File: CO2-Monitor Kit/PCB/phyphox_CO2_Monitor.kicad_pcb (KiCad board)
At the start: 2 copper layers, 73 x 42 mm, 15 parts, among them J1 Conn_01x19_Female, J2 Conn_01x19_Female, J3 Conn_01x05_Female, U1 ESP32-DEVKITC-32D, U2 SCD30

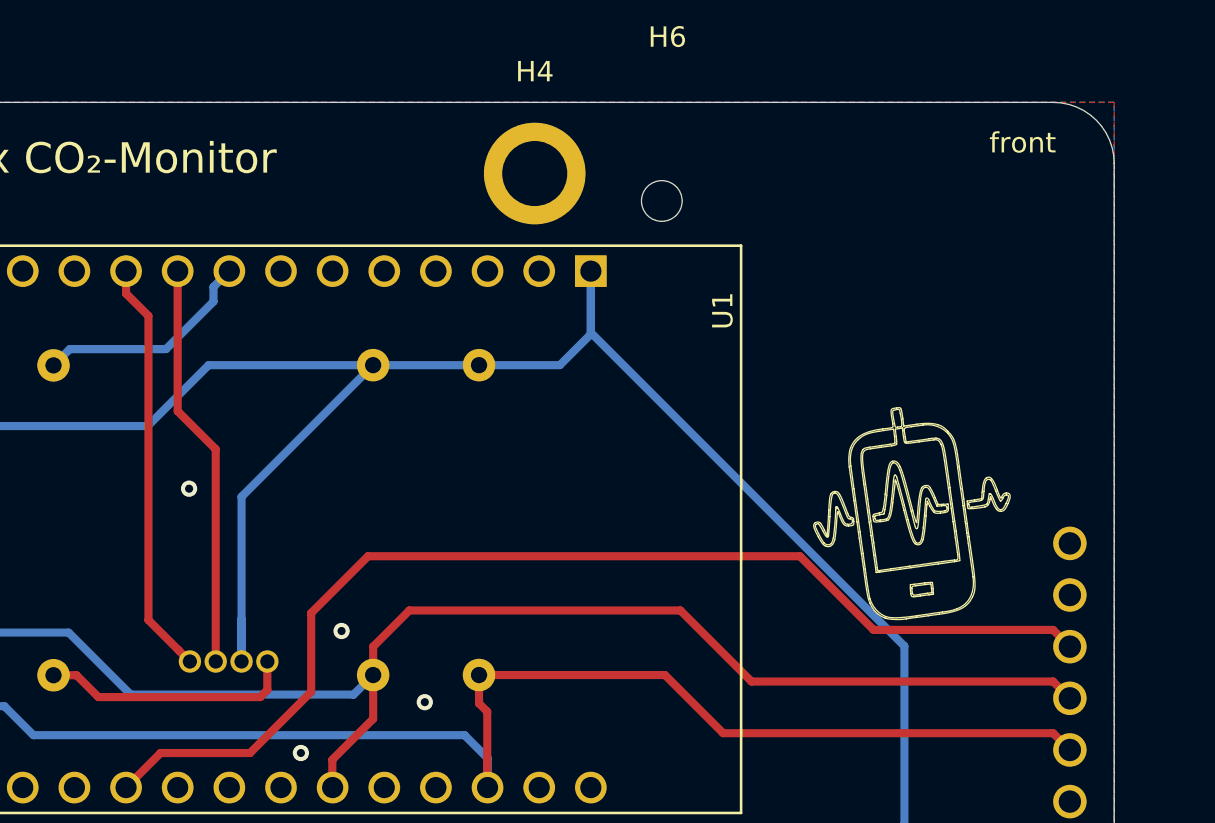
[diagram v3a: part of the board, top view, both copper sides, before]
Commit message: [CO2-Kit] Update PCB to Rev 1.1
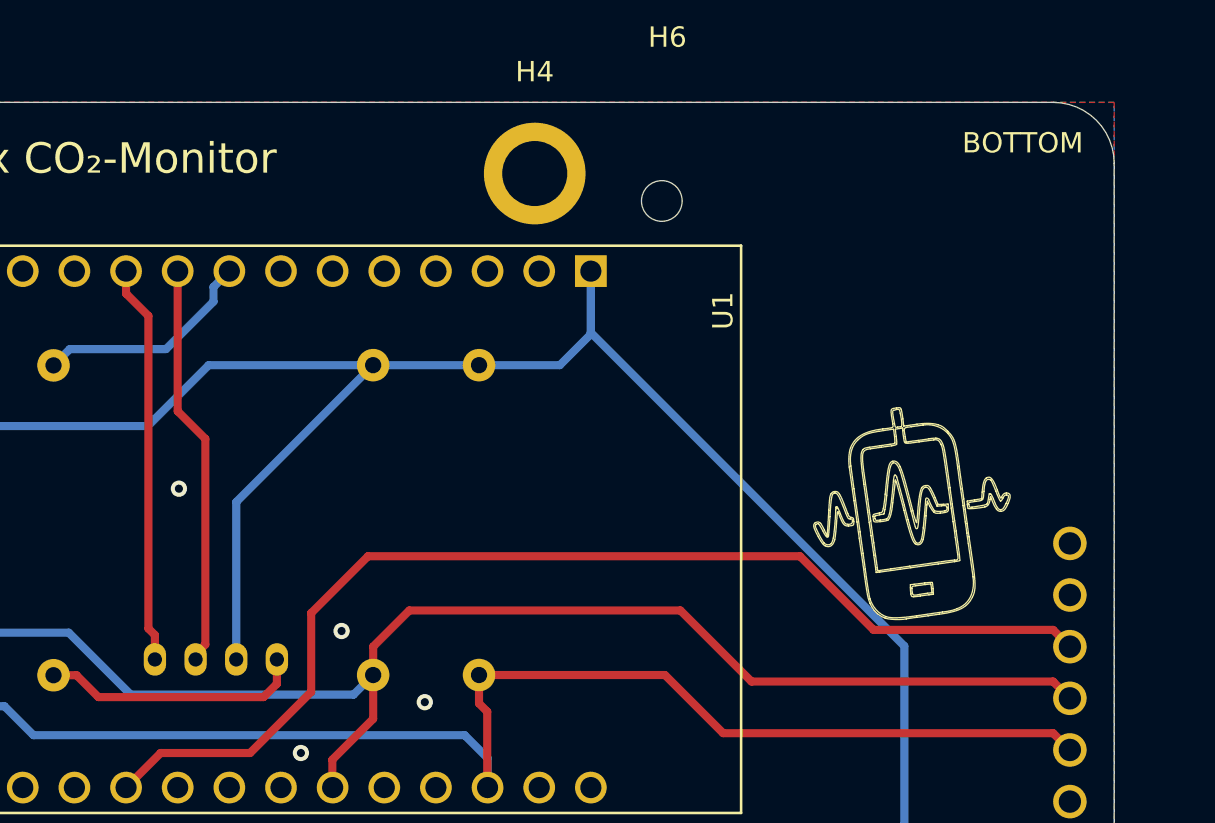
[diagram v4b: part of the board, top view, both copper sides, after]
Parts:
- D1: footprint phyphox_CO2_Monitor:WP154A4SEJ3VBDZGWCA -> phyphox_CO2_Monitor:WP154A4SEJ3VBDZGWCA_largerDistance
- moved D1 0.44 mm to (138.3, 85.1)
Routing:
- net VDD: track 109.2 -> 107.1 mm
- net GREEN: track 20.5 -> 19.7 mm
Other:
- board text added: "BOTTOM"
- board text added: "Rev 1.1"
- board text added: "TOP"
- board text removed: "Rev 1.0"
- board text removed: "back"
- board text removed: "front"
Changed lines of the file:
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@@
     (thickness 1.6)
     (drawings 608)
-    (tracks 88)
+    (tracks 90)
     (zones 0)
     (modules 15)
@@
     (add_net SDA)
     (add_net VDD)
+  )
+  (module phyphox_CO2_Monitor:WP154A4SEJ3VBDZGWCA_largerDistance (layer B.Cu)
+    (at 138.33364 85.09746 90)
+    (fp_text reference D1 (at 0 -0.5 90) (layer B.SilkS)
+      (effects (font (size 1 1) (thickness 0.15)) (justify mirror))
+    )
+    (fp_text value LED_BARG (at 0 0.5 90) (layer B.Fab)
+      (effects (font (size 1 1) (thickness 0.15)) (justify mirror))
+    )
+    (fp_line (start 2 7.999999) (end -1.999999 7.999999) (layer B.SilkS) (width 0.15))
+    (fp_arc (start 0 4.445) (end -1.999999 7.999999) (angle 301.2768412) (layer B.SilkS) (width 0.15))
+    (pad 4 thru_hole oval (at 0 1.25 90) (size 1.6 1.1) (drill 0.7) (layers *.Cu *.Mask)
+      (net 7 GREEN))
+    (pad 3 thru_hole oval (at 0 3.25 90) (size 1.6 1.1) (drill 0.7) (layers *.Cu *.Mask)
+      (net 8 BLUE))
+    (pad 2 thru_hole oval (at 0 5.25 90) (size 1.6 1.1) (drill 0.7) (layers *.Cu *.Mask)
+      (net 2 VDD))
+    (pad 1 thru_hole oval (at 0 7.25 90) (size 1.6 1.1) (drill 0.7) (layers *.Cu *.Mask)
+      (net 1 "Net-(D1-Pad1)"))
   )
   (module MountingHole:MountingHole_2mm (layer F.Cu)
@@
       (net 6 GND))
   )
-  (module phyphox_CO2_Monitor:WP154A4SEJ3VBDZGWCA (layer B.Cu)
-    (at 138.7648 85.1992 90)
-    (fp_text reference D1 (at -3.842 4.628 -90) (layer B.SilkS)
-      (effects (font (size 1 1) (thickness 0.15)) (justify mirror))
-    )
-    (fp_text value LED_BARG (at 0.36 7.65 -90) (layer B.Fab)
-      (effects (font (size 1 1) (thickness 0.15)) (justify mirror))
-    )
-    (fp_line (start 1.27 6.984999) (end -1.269999 6.984999) (layer B.SilkS) (width 0.15))
-    (fp_arc (start 0 4.445) (end -1.269999 6.984999) (angle 306.8698976) (layer B.SilkS) (width 0.15))
-    (pad 4 thru_hole circle (at 0 2.54 90) (size 1.1 1.1) (drill 0.7) (layers *.Cu *.Mask)
-      (net 7 GREEN))
-    (pad 3 thru_hole circle (at 0 3.81 90) (size 1.1 1.1) (drill 0.7) (layers *.Cu *.Mask)
-      (net 8 BLUE))
-    (pad 2 thru_hole circle (at 0 5.08 90) (size 1.1 1.1) (drill 0.7) (layers *.Cu *.Mask)
-      (net 2 VDD))
-    (pad 1 thru_hole circle (at 0 6.35 90) (size 1.1 1.1) (drill 0.7) (layers *.Cu *.Mask)
-      (net 1 "Net-(D1-Pad1)"))
-  )
   (module Connector_PinSocket_2.54mm:PinSocket_1x19_P2.54mm_Vertical (layer F.Cu)
     (at 161.2648 114.6992 270)
@@
     )
   )
-  (gr_text back (at 182.2648 59.6992) (layer B.SilkS)
+  (gr_text TOP (at 182.2648 59.6992) (layer B.SilkS)
     (effects (font (size 1 1) (thickness 0.15)) (justify mirror))
   )
-  (gr_text front (at 182.2648 59.6992) (layer F.SilkS)
+  (gr_text BOTTOM (at 182.2648 59.6992) (layer F.SilkS)
     (effects (font (size 1 1) (thickness 0.15)))
   )
@@
   (gr_curve (pts (xy 147.544591 72.77071) (xy 147.759932 72.77071) (xy 147.787269 72.922918) (xy 147.634671 73.272271)) (layer B.SilkS) (width 0.01))
   (gr_curve (pts (xy 147.634671 73.272271) (xy 147.501108 73.578043) (xy 147.414536 73.67071) (xy 147.262435 73.67071)) (layer B.SilkS) (width 0.01))
-  (gr_text "Rev 1.0" (at 150.4448 96.6592) (layer B.SilkS)
+  (gr_text "Rev 1.1" (at 150.4448 96.6592) (layer B.SilkS)
     (effects (font (size 1.5 1.5) (thickness 0.3)) (justify mirror))
   )
@@
   (segment (start 134.5973 85.8747) (end 135.72867 85.8747) (width 0.4) (layer F.Cu) (net 1))
   (segment (start 136.80317 86.9492) (end 144.7648 86.9492) (width 0.4) (layer F.Cu) (net 1))
-  (segment (start 145.1148 86.5992) (end 145.1148 85.1992) (width 0.4) (layer F.Cu) (net 1))
-  (segment (start 144.7648 86.9492) (end 145.1148 86.5992) (width 0.4) (layer F.Cu) (net 1))
+  (segment (start 144.9319 86.9492) (end 144.7648 86.9492) (width 0.4) (layer F.Cu) (net 1))
+  (segment (start 145.58364 86.29746) (end 144.9319 86.9492) (width 0.4) (layer F.Cu) (net 1))
+  (segment (start 145.58364 85.09746) (end 145.58364 86.29746) (width 0.4) (layer F.Cu) (net 1))
   (segment (start 150.3178 70.6242) (end 155.5248 70.6242) (width 0.4) (layer B.Cu) (net 2))
   (segment (start 155.5248 70.6242) (end 159.4998 70.6242) (width 0.4) (layer B.Cu) (net 2))
   (segment (start 161.0248 69.0992) (end 161.0248 65.9992) (width 0.4) (layer B.Cu) (net 2))
   (segment (start 159.4998 70.6242) (end 161.0248 69.0992) (width 0.4) (layer B.Cu) (net 2))
-  (segment (start 143.8448 83.1042) (end 143.8448 85.1992) (width 0.4) (layer B.Cu) (net 2))
-  (segment (start 143.8448 77.0972) (end 150.3178 70.6242) (width 0.4) (layer B.Cu) (net 2))
-  (segment (start 143.8448 85.1992) (end 143.8448 77.0972) (width 0.4) (layer B.Cu) (net 2))
   (segment (start 161.0248 69.0232) (end 161.0248 65.9992) (width 0.4) (layer B.Cu) (net 2))
   (segment (start 176.4448 84.4432) (end 161.0248 69.0232) (width 0.4) (layer B.Cu) (net 2))
@@
   (segment (start 142.2278 70.6242) (end 150.3178 70.6242) (width 0.4) (layer B.Cu) (net 2))
   (segment (start 139.2328 73.6192) (end 142.2278 70.6242) (width 0.4) (layer B.Cu) (net 2))
+  (segment (start 143.58364 77.35836) (end 143.58364 85.09746) (width 0.4) (layer B.Cu) (net 2))
+  (segment (start 150.3178 70.6242) (end 143.58364 77.35836) (width 0.4) (layer B.Cu) (net 2))
   (segment (start 150.3178 88.0232) (end 150.3178 85.8642) (width 0.4) (layer F.Cu) (net 3))
   (segment (start 148.31 91.376) (end 148.31 90.031) (width 0.4) (layer F.Cu) (net 3))
@@
   (via (at 152.8578 87.1992) (size 0.8) (drill 0.4) (layers F.Cu B.Cu) (net 6))
   (via (at 148.7648 83.6992) (size 0.8) (drill 0.4) (layers F.Cu B.Cu) (net 6))
-  (via (at 141.2648 76.6992) (size 0.8) (drill 0.4) (layers F.Cu B.Cu) (net 6))
+  (via (at 140.7648 76.6992) (size 0.8) (drill 0.4) (layers F.Cu B.Cu) (net 6))
   (via (at 117.2648 71.1992) (size 0.8) (drill 0.4) (layers F.Cu B.Cu) (net 6))
-  (segment (start 140.754801 84.649201) (end 141.3048 85.1992) (width 0.4) (layer F.Cu) (net 7))
-  (segment (start 139.2648 83.1592) (end 140.754801 84.649201) (width 0.4) (layer F.Cu) (net 7))
-  (segment (start 139.2648 68.202286) (end 139.2648 83.1592) (width 0.4) (layer F.Cu) (net 7))
-  (segment (start 138.1648 65.9992) (end 138.1648 67.102286) (width 0.4) (layer F.Cu) (net 7))
-  (segment (start 138.1648 67.102286) (end 139.2648 68.202286) (width 0.4) (layer F.Cu) (net 7))
-  (segment (start 142.5748 85.1992) (end 142.5748 74.7592) (width 0.4) (layer F.Cu) (net 8))
+  (segment (start 138.1648 67.102286) (end 138.1648 65.9992) (width 0.4) (layer F.Cu) (net 7))
+  (segment (start 139.2648 68.202286) (end 138.1648 67.102286) (width 0.4) (layer F.Cu) (net 7))
+  (segment (start 139.2648 83.57862) (end 139.2648 68.202286) (width 0.4) (layer F.Cu) (net 7))
+  (segment (start 139.58364 83.89746) (end 139.2648 83.57862) (width 0.4) (layer F.Cu) (net 7))
+  (segment (start 139.58364 85.09746) (end 139.58364 83.89746) (width 0.4) (layer F.Cu) (net 7))
   (segment (start 140.7048 72.8892) (end 140.7048 65.9992) (width 0.4) (layer F.Cu) (net 8))
-  (segment (start 142.5748 74.7592) (end 140.7048 72.8892) (width 0.4) (layer F.Cu) (net 8))
+  (segment (start 142.064801 74.249201) (end 140.7048 72.8892) (width 0.4) (layer F.Cu) (net 8))
+  (segment (start 142.064801 84.366299) (end 142.064801 74.249201) (width 0.4) (layer F.Cu) (net 8))
+  (segment (start 141.58364 84.84746) (end 142.064801 84.366299) (width 0.4) (layer F.Cu) (net 8))
+  (segment (start 141.58364 85.09746) (end 141.58364 84.84746) (width 0.4) (layer F.Cu) (net 8))
   (segment (start 143.2058 66.0002) (end 143.23 65.976) (width 0.4) (layer F.Cu) (net 9))
   (segment (start 135.397299 69.834701) (end 140.129299 69.834701) (width 0.4) (layer B.Cu) (net 9))
@@
   (segment (start 125.4648 91.3992) (end 125.4648 90.296114) (width 0.4) (layer B.Cu) (net 40))
   (segment (start 125.4648 90.296114) (end 120.2648 85.096114) (width 0.4) (layer B.Cu) (net 40))
-  (zone (net 6) (net_name GND) (layer F.Cu) (hatch edge 0.508)
-    (connect_pads (clearance 0.508))
-    (min_thickness 0.254)
-    (fill yes (arc_segments 32) (thermal_gap 0.508) (thermal_bridge_width 0.508))
-    (polygon
-      (pts
-        (xy 113.7648 99.6992) (xy 113.7648 57.6992) (xy 186.7648 57.6992) (xy 186.7648 99.6992)
-      )
-    )
-  )
   (zone (net 6) (net_name GND) (layer B.Cu) (hatch edge 0.508)
     (connect_pads (clearance 0.508))
@@
       )
     )
+  )
+  (zone (net 6) (net_name GND) (layer F.Cu) (hatch edge 0.508)
+    (connect_pads (clearance 0.508))
+    (min_thickness 0.254)
+    (fill yes (arc_segments 32) (thermal_gap 0.508) (thermal_bridge_width 0.508))
+    (polygon
+      (pts
+        (xy 113.7648 57.6992) (xy 186.7648 57.6992) (xy 186.7648 99.6992) (xy 113.7648 99.6992)
+      )
+    )

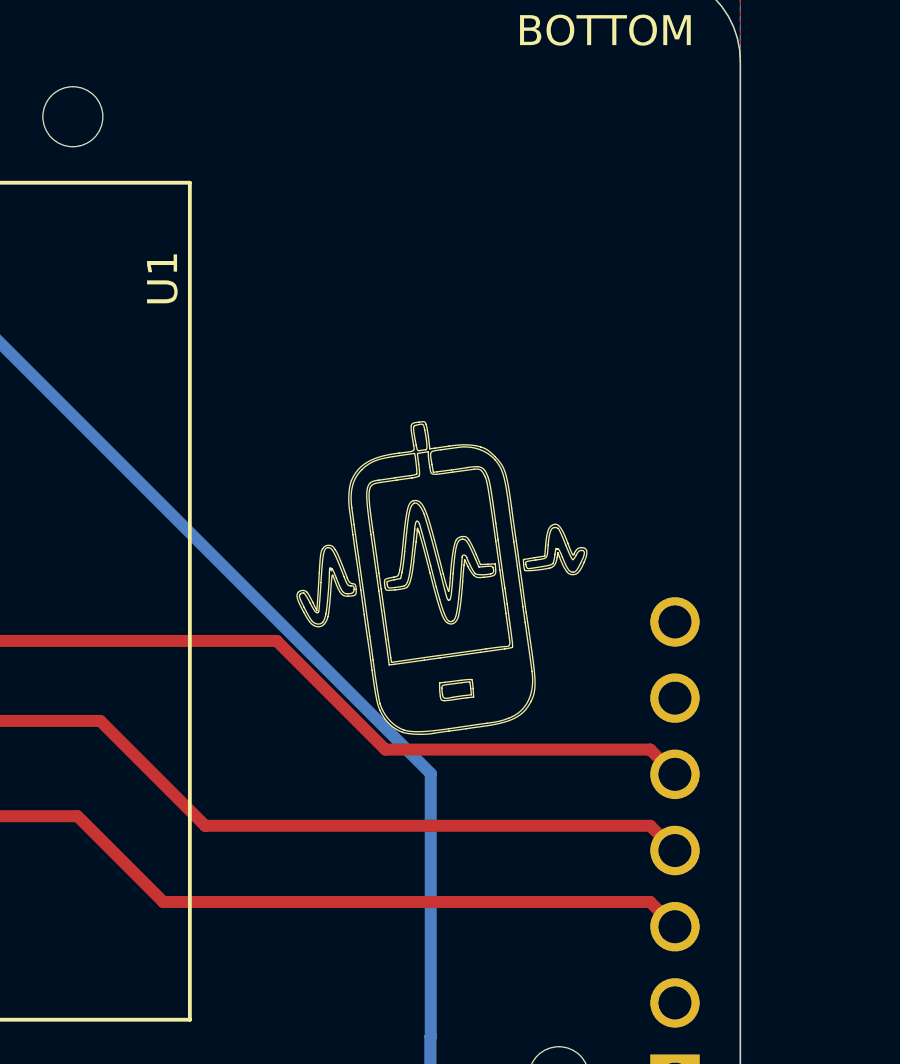
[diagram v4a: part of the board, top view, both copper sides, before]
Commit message: Silkscreen updated
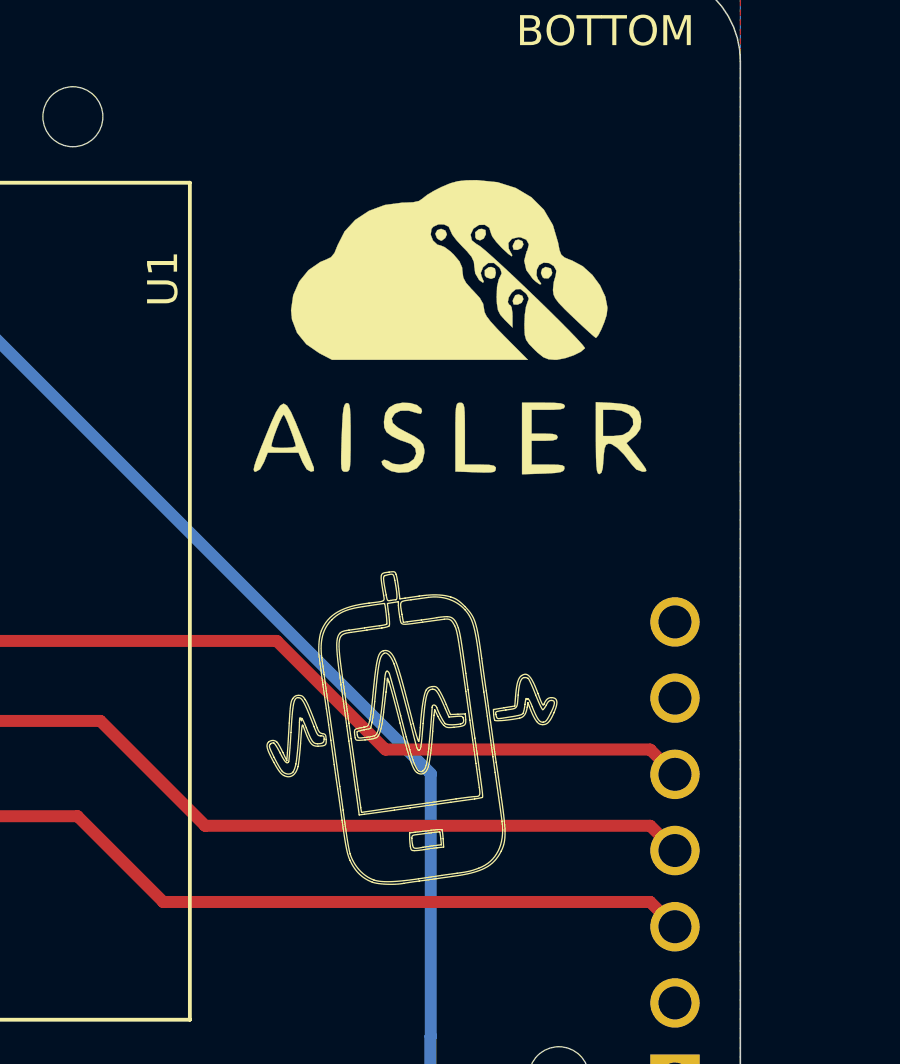
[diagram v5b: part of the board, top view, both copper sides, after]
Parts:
- added G***: LOGO, phyphox_CO2_Monitor:aisler_15x12mm, B.Cu at (174.3, 69.7)
- added G***: LOGO, phyphox_CO2_Monitor:aisler_15x12mm, F.Cu at (177.3, 69.7)
